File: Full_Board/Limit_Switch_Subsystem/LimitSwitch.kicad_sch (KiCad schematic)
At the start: 6 parts, among them J5 OQ0212500000G

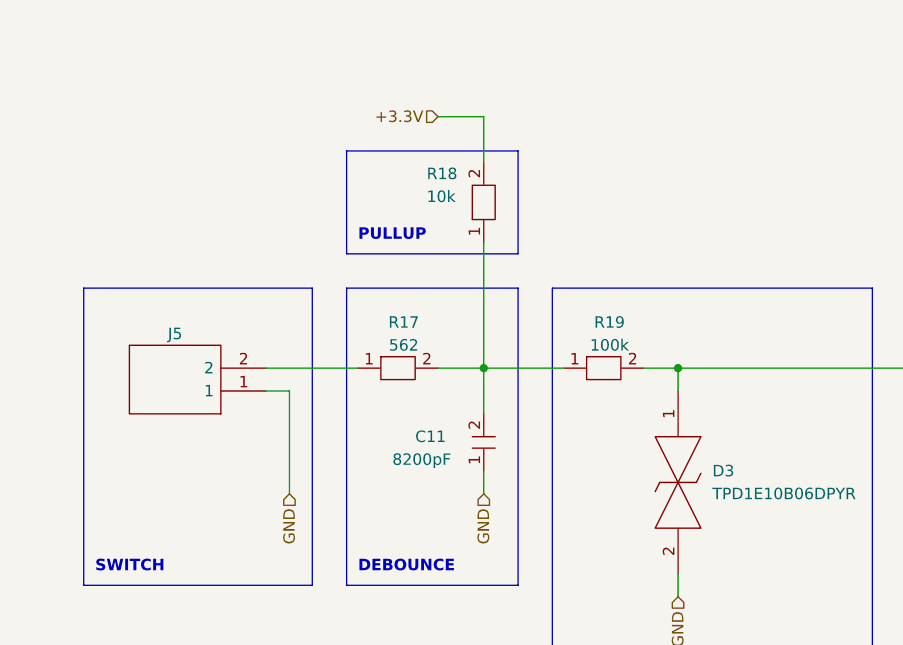
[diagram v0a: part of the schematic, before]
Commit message: Add screenshots of each subsystem
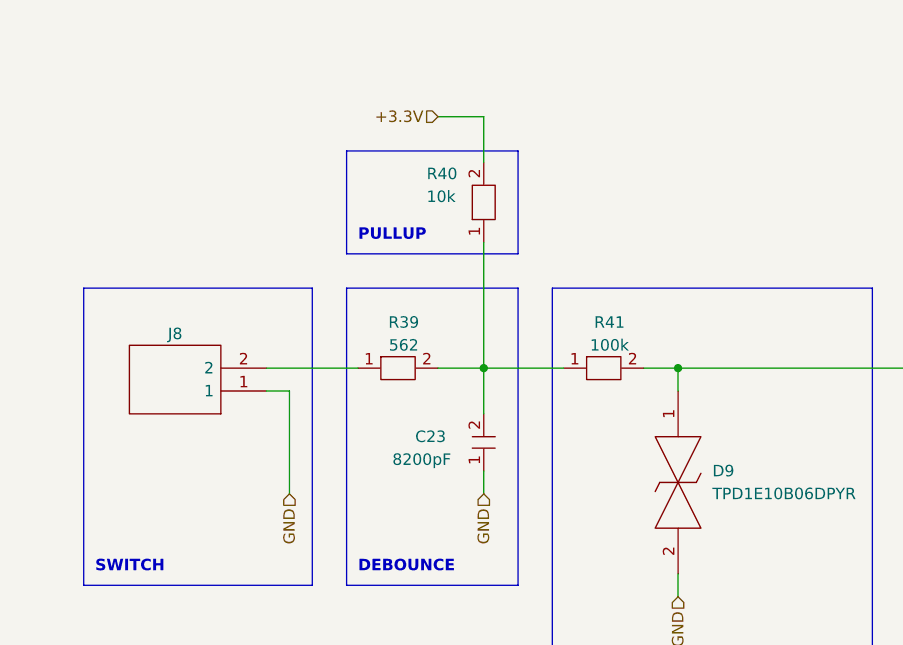
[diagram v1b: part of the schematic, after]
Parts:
- renumbered C11 to C23, D3 to D9, J5 to J8, R17 to R39, R18 to R40, R19 to R41
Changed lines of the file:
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@@
   (symbol (lib_id "OQ0212500000G:OQ0212500000G") (at 119.38 92.71 180) (unit 1)
     (in_bom yes) (on_board yes)
-    (property "Reference" "J5" (id 0) (at 109.22 86.36 0))
+    (property "Reference" "J8" (id 0) (at 109.22 86.36 0))
     (property "Value" "OQ0212500000G" (id 1) (at 109.22 85.09 0)
       (effects (font (size 1.27 1.27)) hide)
@@
   (symbol (lib_id "CR0402-FX-5620GLF:CR0402-FX-5620GLF") (at 129.54 90.17 0) (unit 1)
     (in_bom yes) (on_board yes)
-    (property "Reference" "R17" (id 0) (at 134.62 85.09 0))
+    (property "Reference" "R39" (id 0) (at 134.62 85.09 0))
     (property "Value" "562" (id 1) (at 134.62 87.63 0))
     (property "Footprint" "CR0402-FX-5620GLF:RESC1005X40N" (id 2) (at 143.51 88.9 0)
@@
   (symbol (lib_id "C1210C822K2RACAUTO:8200pF") (at 143.51 101.6 90) (unit 1)
     (in_bom yes) (on_board yes)
-    (property "Reference" "C11" (id 0) (at 135.89 97.79 90)
+    (property "Reference" "C23" (id 0) (at 135.89 97.79 90)
       (effects (font (size 1.27 1.27)) (justify right))
     )
@@
   (symbol (lib_id "RCV2512100KFKEGAT:RCV2512100KFKEGAT") (at 152.4 90.17 0) (unit 1)
     (in_bom yes) (on_board yes)
-    (property "Reference" "R19" (id 0) (at 157.48 85.09 0))
+    (property "Reference" "R41" (id 0) (at 157.48 85.09 0))
     (property "Value" "100k" (id 1) (at 157.48 87.63 0))
     (property "Footprint" "RCV2512100KFKEGAT:RESC6332X70N" (id 2) (at 166.37 88.9 0)
@@
   (symbol (lib_id "CRMA1210AF10K0DKEF:10k") (at 143.51 76.2 90) (unit 1)
     (in_bom yes) (on_board yes)
-    (property "Reference" "R18" (id 0) (at 137.16 68.58 90)
+    (property "Reference" "R40" (id 0) (at 137.16 68.58 90)
       (effects (font (size 1.27 1.27)) (justify right))
     )
@@
   (symbol (lib_id "TPD1E10B06DPYR:TPD1E10B06DPYR") (at 165.1 92.71 270) (unit 1)
     (in_bom yes) (on_board yes)
-    (property "Reference" "D3" (id 0) (at 168.91 101.6 90)
+    (property "Reference" "D9" (id 0) (at 168.91 101.6 90)
       (effects (font (size 1.27 1.27)) (justify left))
     )

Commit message: Added 5V power supply
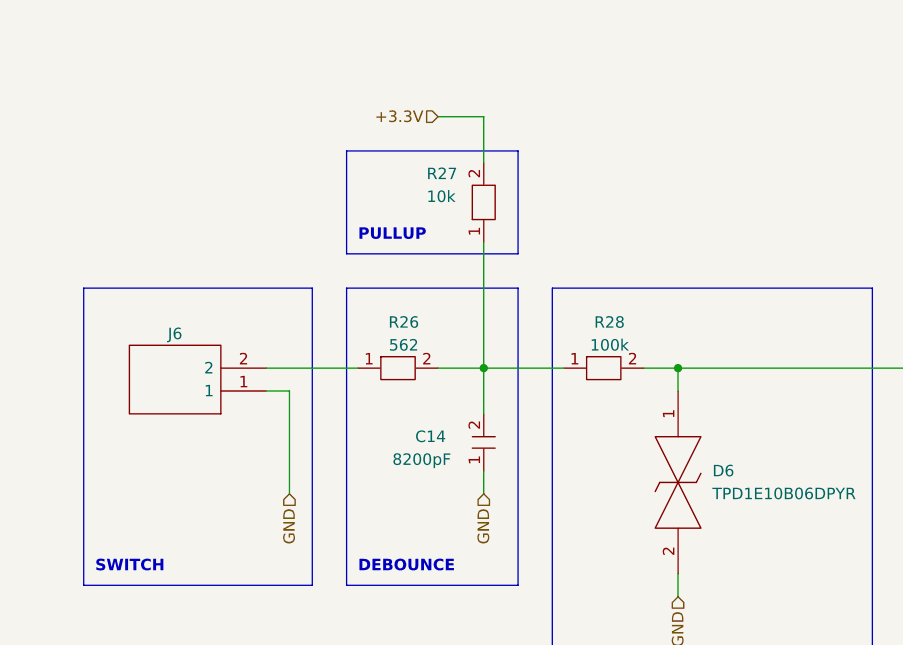
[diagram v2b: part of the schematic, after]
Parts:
- renumbered C23 to C14, D9 to D6, J8 to J6, R39 to R26, R40 to R27, R41 to R28
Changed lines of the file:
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@@
     (effects (font (size 1.27 1.27)) (justify right))
   )
-  (symbol (lib_id "OQ0212500000G:OQ0212500000G") (at 119.38 92.71 180) (unit 1)
+  (symbol (lib_id "OQ0212500000G:OQ0212500000G") (at 119.38 92.71 180)
     (in_bom yes) (on_board yes)
-    (property "Reference" "J8" (id 0) (at 109.22 86.36 0))
+    (property "Reference" "J6" (id 0) (at 109.22 86.36 0))
     (property "Value" "OQ0212500000G" (id 1) (at 109.22 85.09 0)
       (effects (font (size 1.27 1.27)) hide)
@@
     (pin "2")
   )
-  (symbol (lib_id "CR0402-FX-5620GLF:CR0402-FX-5620GLF") (at 129.54 90.17 0) (unit 1)
+  (symbol (lib_id "CR0402-FX-5620GLF:CR0402-FX-5620GLF") (at 129.54 90.17 0)
     (in_bom yes) (on_board yes)
-    (property "Reference" "R39" (id 0) (at 134.62 85.09 0))
+    (property "Reference" "R26" (id 0) (at 134.62 85.09 0))
     (property "Value" "562" (id 1) (at 134.62 87.63 0))
     (property "Footprint" "CR0402-FX-5620GLF:RESC1005X40N" (id 2) (at 143.51 88.9 0)
@@
     (pin "2")
   )
-  (symbol (lib_id "C1210C822K2RACAUTO:8200pF") (at 143.51 101.6 90) (unit 1)
+  (symbol (lib_id "C1210C822K2RACAUTO:8200pF") (at 143.51 101.6 90)
     (in_bom yes) (on_board yes)
-    (property "Reference" "C23" (id 0) (at 135.89 97.79 90)
+    (property "Reference" "C14" (id 0) (at 135.89 97.79 90)
       (effects (font (size 1.27 1.27)) (justify right))
     )
@@
     (pin "2")
   )
-  (symbol (lib_id "RCV2512100KFKEGAT:RCV2512100KFKEGAT") (at 152.4 90.17 0) (unit 1)
+  (symbol (lib_id "RCV2512100KFKEGAT:RCV2512100KFKEGAT") (at 152.4 90.17 0)
     (in_bom yes) (on_board yes)
-    (property "Reference" "R41" (id 0) (at 157.48 85.09 0))
+    (property "Reference" "R28" (id 0) (at 157.48 85.09 0))
     (property "Value" "100k" (id 1) (at 157.48 87.63 0))
     (property "Footprint" "RCV2512100KFKEGAT:RESC6332X70N" (id 2) (at 166.37 88.9 0)
@@
     (pin "2")
   )
-  (symbol (lib_id "CRMA1210AF10K0DKEF:10k") (at 143.51 76.2 90) (unit 1)
+  (symbol (lib_id "CRMA1210AF10K0DKEF:10k") (at 143.51 76.2 90)
     (in_bom yes) (on_board yes)
-    (property "Reference" "R40" (id 0) (at 137.16 68.58 90)
+    (property "Reference" "R27" (id 0) (at 137.16 68.58 90)
       (effects (font (size 1.27 1.27)) (justify right))
     )
@@
     (pin "2")
   )
-  (symbol (lib_id "TPD1E10B06DPYR:TPD1E10B06DPYR") (at 165.1 92.71 270) (unit 1)
+  (symbol (lib_id "TPD1E10B06DPYR:TPD1E10B06DPYR") (at 165.1 92.71 270)
     (in_bom yes) (on_board yes)
-    (property "Reference" "D9" (id 0) (at 168.91 101.6 90)
+    (property "Reference" "D6" (id 0) (at 168.91 101.6 90)
       (effects (font (size 1.27 1.27)) (justify left))
     )

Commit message: Added extra bypass caps to the power supply
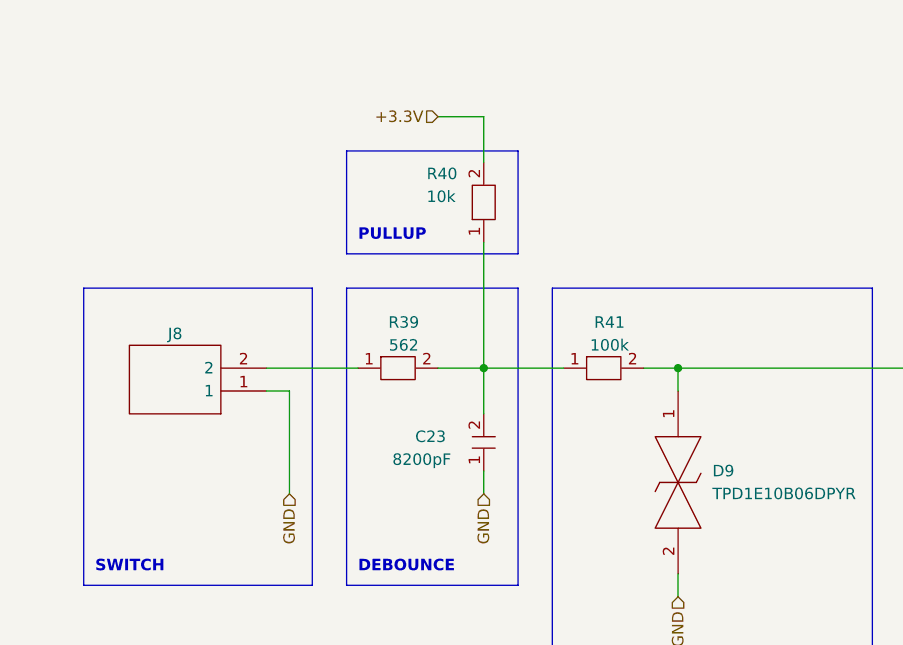
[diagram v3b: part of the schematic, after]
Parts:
- renumbered C14 to C23, D6 to D9, J6 to J8, R26 to R39, R27 to R40, R28 to R41
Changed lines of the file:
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@@
   (symbol (lib_id "OQ0212500000G:OQ0212500000G") (at 119.38 92.71 180)
     (in_bom yes) (on_board yes)
-    (property "Reference" "J6" (id 0) (at 109.22 86.36 0))
+    (property "Reference" "J8" (id 0) (at 109.22 86.36 0))
     (property "Value" "OQ0212500000G" (id 1) (at 109.22 85.09 0)
       (effects (font (size 1.27 1.27)) hide)
@@
   (symbol (lib_id "CR0402-FX-5620GLF:CR0402-FX-5620GLF") (at 129.54 90.17 0)
     (in_bom yes) (on_board yes)
-    (property "Reference" "R26" (id 0) (at 134.62 85.09 0))
+    (property "Reference" "R39" (id 0) (at 134.62 85.09 0))
     (property "Value" "562" (id 1) (at 134.62 87.63 0))
     (property "Footprint" "CR0402-FX-5620GLF:RESC1005X40N" (id 2) (at 143.51 88.9 0)
@@
   (symbol (lib_id "C1210C822K2RACAUTO:8200pF") (at 143.51 101.6 90)
     (in_bom yes) (on_board yes)
-    (property "Reference" "C14" (id 0) (at 135.89 97.79 90)
+    (property "Reference" "C23" (id 0) (at 135.89 97.79 90)
       (effects (font (size 1.27 1.27)) (justify right))
     )
@@
   (symbol (lib_id "RCV2512100KFKEGAT:RCV2512100KFKEGAT") (at 152.4 90.17 0)
     (in_bom yes) (on_board yes)
-    (property "Reference" "R28" (id 0) (at 157.48 85.09 0))
+    (property "Reference" "R41" (id 0) (at 157.48 85.09 0))
     (property "Value" "100k" (id 1) (at 157.48 87.63 0))
     (property "Footprint" "RCV2512100KFKEGAT:RESC6332X70N" (id 2) (at 166.37 88.9 0)
@@
   (symbol (lib_id "CRMA1210AF10K0DKEF:10k") (at 143.51 76.2 90)
     (in_bom yes) (on_board yes)
-    (property "Reference" "R27" (id 0) (at 137.16 68.58 90)
+    (property "Reference" "R40" (id 0) (at 137.16 68.58 90)
       (effects (font (size 1.27 1.27)) (justify right))
     )
@@
   (symbol (lib_id "TPD1E10B06DPYR:TPD1E10B06DPYR") (at 165.1 92.71 270)
     (in_bom yes) (on_board yes)
-    (property "Reference" "D6" (id 0) (at 168.91 101.6 90)
+    (property "Reference" "D9" (id 0) (at 168.91 101.6 90)
       (effects (font (size 1.27 1.27)) (justify left))
     )

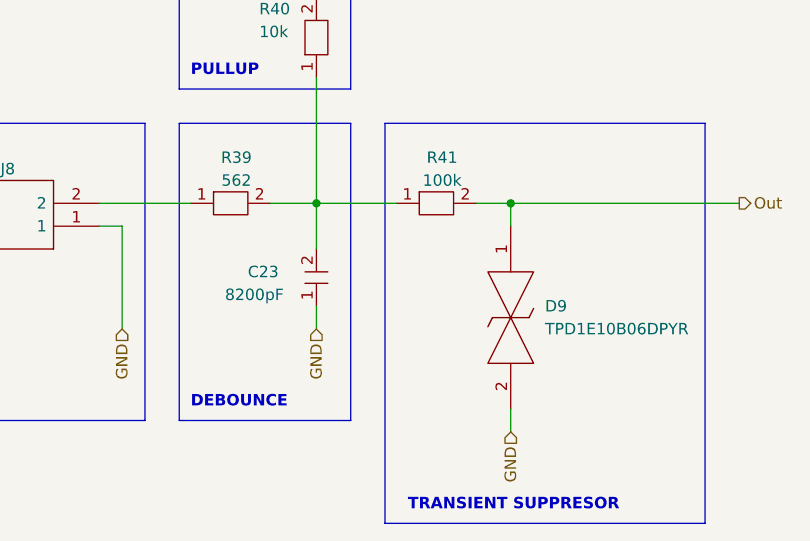
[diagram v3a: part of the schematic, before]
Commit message: Merge Eli and Gabi files. Remove unecessary ECAD remnants. Update stepper components post-part order
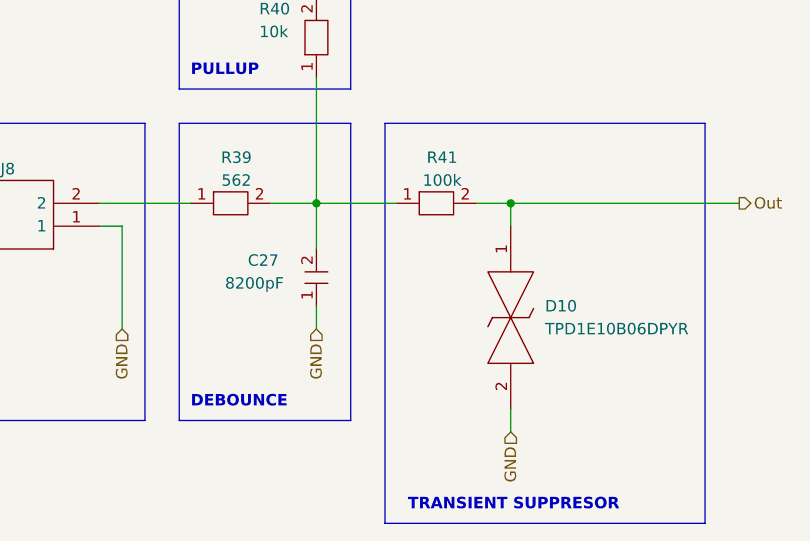
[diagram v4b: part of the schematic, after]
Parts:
- removed C23: 8200pF, C1210C822K2RACAUTO:CAPC3225X88N, symbol C1210C822K2RACAUTO:8200pF
- removed R40: 10k, CRMA1210AF10K0DKEF:RESC3225X74N, symbol CRMA1210AF10K0DKEF:10k
- added C27: 8200pF, C1210C822K2RACAUTO:CAPC3225X88N, symbol C1210C822K2RACAUTO:C1210C822K2RACAUTO
- added R40: 10k, RESC3225X74N, symbol RMCF1206FT10K0:10k
- J8: Digikey Link (none) -> https://www.digikey.com/en/products/detail/amphenol-anytek/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; Manufacturer_Part_Number (none) -> OQ0212500000G; Mouser Price/Stock (none) -> https://www.mouser.co.uk/ProductDetail/Amphenol-Anytek/OQ02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
- R39: Mouse link (none) -> https://www.mouser.com/ProductDetail/Bourns/CR0402-FX-5620G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
- renumbered D9 to D10
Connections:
- net +3.3V: now also R40.2
- net GND: now also C27.1
- net at R39.2, R41.1: now also C27.2, R40.1
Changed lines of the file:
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@@
     (effects (font (size 1.27 1.27)) (justify right))
   )
-  (symbol (lib_id "OQ0212500000G:OQ0212500000G") (at 119.38 92.71 180)
+  (symbol (lib_id "OQ0212500000G:OQ0212500000G") (at 119.38 92.71 180) (unit 1)
     (in_bom yes) (on_board yes)
     (property "Reference" "J8" (id 0) (at 109.22 86.36 0))
@@
       (effects (font (size 1.27 1.27)) (justify left) hide)
     )
-    (property "Manufacturer_Part_Number" "" (id 4) (at 102.87 77.47 0)
+    (property "Manufacturer_Part_Number" "OQ0212500000G" (id 4) (at 102.87 77.47 0)
       (effects (font (size 1.27 1.27)) (justify left) hide)
     )
@@
       (effects (font (size 1.27 1.27)) (justify left) hide)
     )
-    (property "Digikey Link" "" (id 7) (at 119.38 92.71 0)
+    (property "Digikey Link" "https://www.digikey.com/en/products/detail/amphenol-anytek/OQ0212500000G/4242016" (id 7) (at 119.38 92.71 0)
       (effects (font (size 1.27 1.27)) hide)
     )
@@
       (effects (font (size 1.27 1.27)) (justify left) hide)
     )
-    (property "Mouser Price/Stock" "" (id 11) (at 102.87 82.55 0)
+    (property "Mouser Price/Stock" "https://www.mouser.co.uk/ProductDetail/Amphenol-Anytek/OQ0212500000G?qs=Mv7BduZupUhn3%2FKe8nJdbQ%3D%3D" (id 11) (at 102.87 82.55 0)
       (effects (font (size 1.27 1.27)) (justify left) hide)
     )
@@
     (pin "2")
   )
-  (symbol (lib_id "CR0402-FX-5620GLF:CR0402-FX-5620GLF") (at 129.54 90.17 0)
+  (symbol (lib_id "CR0402-FX-5620GLF:CR0402-FX-5620GLF") (at 129.54 90.17 0) (unit 1)
     (in_bom yes) (on_board yes)
     (property "Reference" "R39" (id 0) (at 134.62 85.09 0))
@@
       (effects (font (size 1.27 1.27)) (justify left) hide)
     )
-    (property "Mouse link" "" (id 8) (at 143.51 104.14 0)
+    (property "Mouse link" "https://www.mouser.com/ProductDetail/Bourns/CR0402-FX-5620GLF?qs=sGAEpiMZZMtlubZbdhIBIDfFWzqdPB9%252B4rUQL12%252Bb9s%3D" (id 8) (at 143.51 104.14 0)
       (effects (font (size 1.27 1.27)) (justify left) hide)
     )
@@
     (pin "2")
   )
-  (symbol (lib_id "C1210C822K2RACAUTO:8200pF") (at 143.51 101.6 90)
+  (symbol (lib_id "RMCF1206FT10K0:10k") (at 143.51 76.2 90) (unit 1)
     (in_bom yes) (on_board yes)
-    (property "Reference" "C23" (id 0) (at 135.89 97.79 90)
+    (property "Reference" "R40" (id 0) (at 137.16 68.58 90)
       (effects (font (size 1.27 1.27)) (justify right))
     )
-    (property "Value" "8200pF" (id 1) (at 133.35 100.33 90)
+    (property "Value" "10k" (id 1) (at 137.16 71.12 90)
       (effects (font (size 1.27 1.27)) (justify right))
     )
-    (property "Footprint" "C1210C822K2RACAUTO:CAPC3225X88N" (id 2) (at 142.24 92.71 0)
+    (property "Footprint" "RESC3225X74N" (id 2) (at 142.24 62.23 0)
       (effects (font (size 1.27 1.27)) (justify left) hide)
     )
-    (property "Datasheet" "https://content.kemet.com/datasheets/KEM_C1023_X7R_AUTO_SMD.pdf" (id 3) (at 144.78 92.71 0)
+    (property "Datasheet" "https://www.vishay.com/docs/68043/crma.pdf" (id 3) (at 144.78 62.23 0)
       (effects (font (size 1.27 1.27)) (justify left) hide)
     )
-    (property "Manufacturer's Part Number" "C1210C822K2RACAUTO" (id 4) (at 160.02 92.71 0)
+    (property "Manufacturer's Part Number" "RMCF1206FT10K0" (id 4) (at 147.32 62.23 0)
       (effects (font (size 1.27 1.27)) (justify left) hide)
     )
-    (property "Digikey Part Number" "399-C1210C822K2RACAUTOCT-ND" (id 5) (at 147.32 92.71 0)
+    (property "Digikey Part Number" "RMCF1206FT10K0CT-ND" (id 5) (at 149.86 62.23 0)
       (effects (font (size 1.27 1.27)) (justify left) hide)
     )
-    (property "Mouser Part Number" "80-C1210C822K2RAUTO" (id 6) (at 152.4 92.71 0)
+    (property "Mouser Part Number" "" (id 6) (at 152.4 62.23 0)
       (effects (font (size 1.27 1.27)) (justify left) hide)
     )
-    (property "Digikey link" "https://www.digikey.com/en/products/detail/kemet/C1210C822K2RACAUTO/16524786?s=N4IgTCBcDaIMIEYwIAxwBxjAaTAJQEE4CBVAFQHkACEAXQF8g" (id 7) (at 154.94 92.71 0)
+    (property "Digikey link" "https://www.digikey.com/en/products/detail/stackpole-electronics-inc/RMCF1206FT10K0/1759669?s=N4IgTCBcDaIEoFkDCAxAjGADANhQFTUwGlMQBdAXyA" (id 7) (at 154.94 62.23 0)
       (effects (font (size 1.27 1.27)) (justify left) hide)
     )
-    (property "Mouser link" "https://www.mouser.com/ProductDetail/KEMET/C1210C822K2RACAUTO?qs=sGAEpiMZZMukHu%252BjC5l7YfRfrXj%2FJXIdfvr9FKYreLc%3D" (id 8) (at 157.48 92.71 0)
+    (property "Mouser link" "" (id 8) (at 157.48 62.23 0)
       (effects (font (size 1.27 1.27)) (justify left) hide)
     )
@@
     (pin "2")
   )
-  (symbol (lib_id "RCV2512100KFKEGAT:RCV2512100KFKEGAT") (at 152.4 90.17 0)
+  (symbol (lib_id "RCV2512100KFKEGAT:RCV2512100KFKEGAT") (at 152.4 90.17 0) (unit 1)
     (in_bom yes) (on_board yes)
     (property "Reference" "R41" (id 0) (at 157.48 85.09 0))
@@
     (pin "2")
   )
-  (symbol (lib_id "CRMA1210AF10K0DKEF:10k") (at 143.51 76.2 90)
+  (symbol (lib_id "C1210C822K2RACAUTO:C1210C822K2RACAUTO") (at 143.51 101.6 90) (unit 1)
     (in_bom yes) (on_board yes)
-    (property "Reference" "R40" (id 0) (at 137.16 68.58 90)
+    (property "Reference" "C27" (id 0) (at 135.89 96.52 90)
       (effects (font (size 1.27 1.27)) (justify right))
     )
-    (property "Value" "10k" (id 1) (at 137.16 71.12 90)
+    (property "Value" "8200pF" (id 1) (at 133.35 99.06 90)
       (effects (font (size 1.27 1.27)) (justify right))
     )
-    (property "Footprint" "CRMA1210AF10K0DKEF:RESC3225X74N" (id 2) (at 142.24 62.23 0)
+    (property "Footprint" "C1210C822K2RACAUTO:CAPC3225X88N" (id 2) (at 142.24 92.71 0)
       (effects (font (size 1.27 1.27)) (justify left) hide)
     )
-    (property "Datasheet" "https://www.vishay.com/docs/68043/crma.pdf" (id 3) (at 144.78 62.23 0)
+    (property "Datasheet" "https://content.kemet.com/datasheets/KEM_C1023_X7R_AUTO_SMD.pdf" (id 3) (at 144.78 92.71 0)
       (effects (font (size 1.27 1.27)) (justify left) hide)
     )
-    (property "Manufacturer's Part Number" "CRMA1210AF10K0DKEF" (id 4) (at 160.02 62.23 0)
+    (property "Manufacturer's Part Number" "C1210C822K2RACAUTO" (id 4) (at 160.02 92.71 0)
       (effects (font (size 1.27 1.27)) (justify left) hide)
     )
-    (property "Digikey Part Number" "3579-CRMA1210AF10K0FKEFCT-ND" (id 5) (at 147.32 62.23 0)
+    (property "Digikey Part Number" "399-C1210C822K2RACAUTOCT-ND" (id 5) (at 147.32 92.71 0)
       (effects (font (size 1.27 1.27)) (justify left) hide)
     )
-    (property "Mouser Part Number" "71-CRMA1210AF10K0DKF" (id 6) (at 152.4 62.23 0)
+    (property "Mouser Part Number" "80-C1210C822K2RAUTO" (id 6) (at 152.4 92.71 0)
       (effects (font (size 1.27 1.27)) (justify left) hide)
     )
-    (property "Digikey link" "https://www.digikey.com/en/products/detail/vishay-techno/CRMA1210AF10K0FKEF/13998641?s=N4IgTCBcDaIMYCcC2BDAjGNAGFAzbA1lrgQKa4gC6AvkA" (id 7) (at 157.48 62.23 0)
+    (property "Digikey link" "https://www.digikey.com/en/products/detail/kemet/C1210C822K2RACAUTO/16524786?s=N4IgTCBcDaIMIEYwIAxwBxjAaTAJQEE4CBVAFQHkACEAXQF8g" (id 7) (at 154.94 92.71 0)
       (effects (font (size 1.27 1.27)) (justify left) hide)
     )
-    (property "Mouser link" "https://www.mouser.com/ProductDetail/Vishay/CRMA1210AF10K0DKEF?qs=sGAEpiMZZMtlubZbdhIBIOn2mbhvx7T2LeIdSPdAQ6k%3D" (id 8) (at 154.94 62.23 0)
+    (property "Mouser link" "https://www.mouser.com/ProductDetail/KEMET/C1210C822K2RACAUTO?qs=sGAEpiMZZMukHu%252BjC5l7YfRfrXj%2FJXIdfvr9FKYreLc%3D" (id 8) (at 157.48 92.71 0)
       (effects (font (size 1.27 1.27)) (justify left) hide)
     )
@@
     (pin "2")
   )
-  (symbol (lib_id "TPD1E10B06DPYR:TPD1E10B06DPYR") (at 165.1 92.71 270)
+  (symbol (lib_id "TPD1E10B06DPYR:TPD1E10B06DPYR") (at 165.1 92.71 270) (unit 1)
     (in_bom yes) (on_board yes)
-    (property "Reference" "D9" (id 0) (at 168.91 101.6 90)
+    (property "Reference" "D10" (id 0) (at 168.91 101.6 90)
       (effects (font (size 1.27 1.27)) (justify left))
     )
